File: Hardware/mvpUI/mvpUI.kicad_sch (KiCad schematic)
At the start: 0 parts

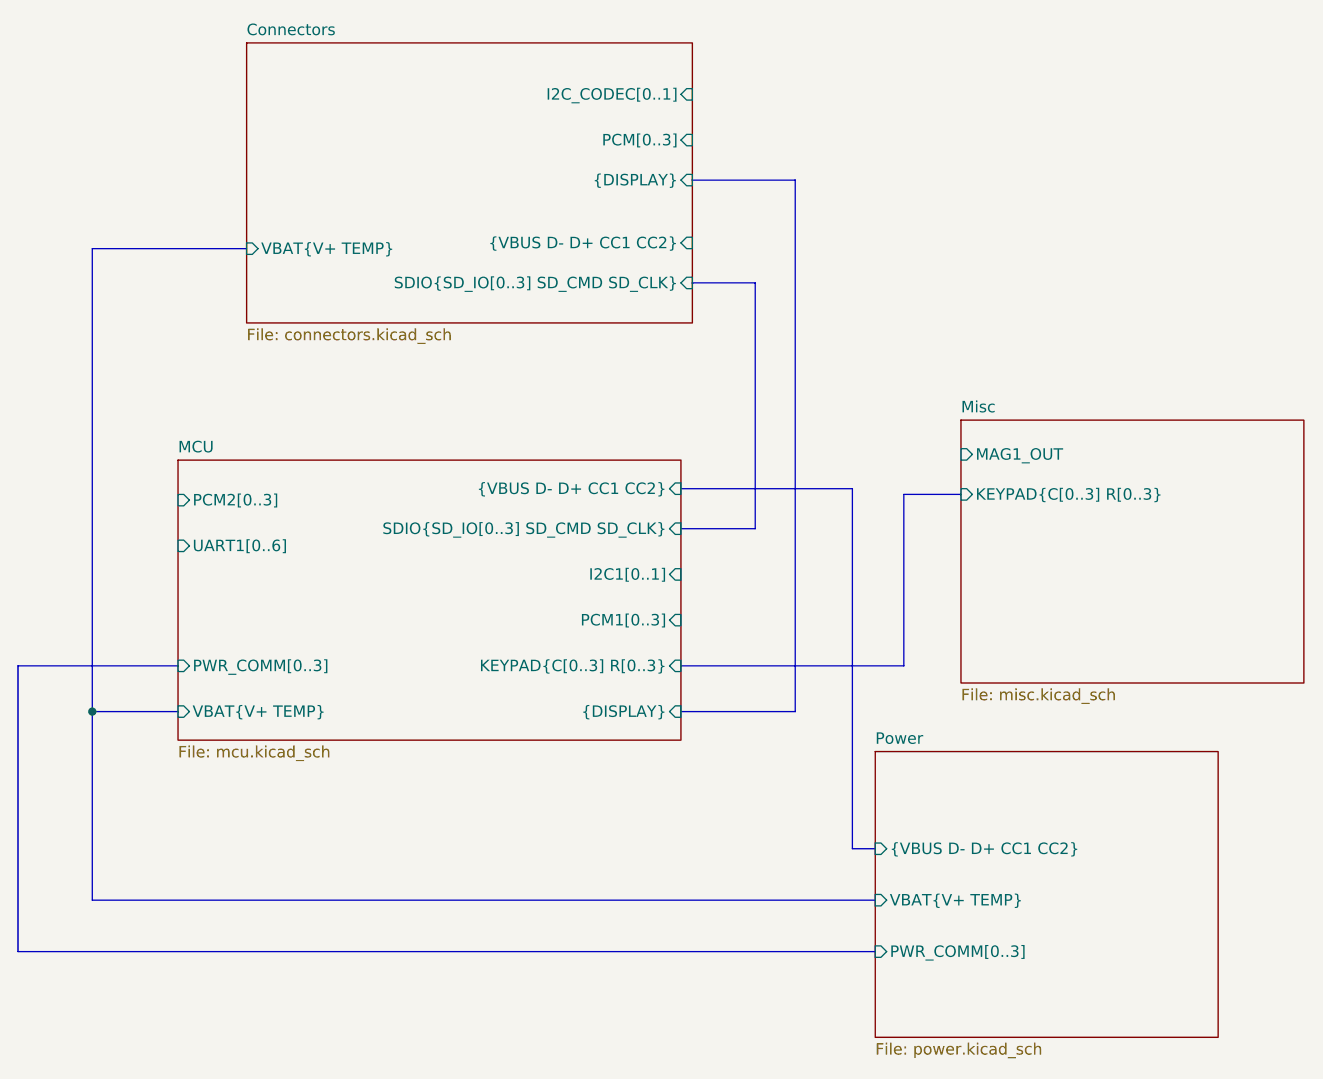
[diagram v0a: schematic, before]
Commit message: Getting there...
Just need logic and power planes for the most part (and verify everything once more)
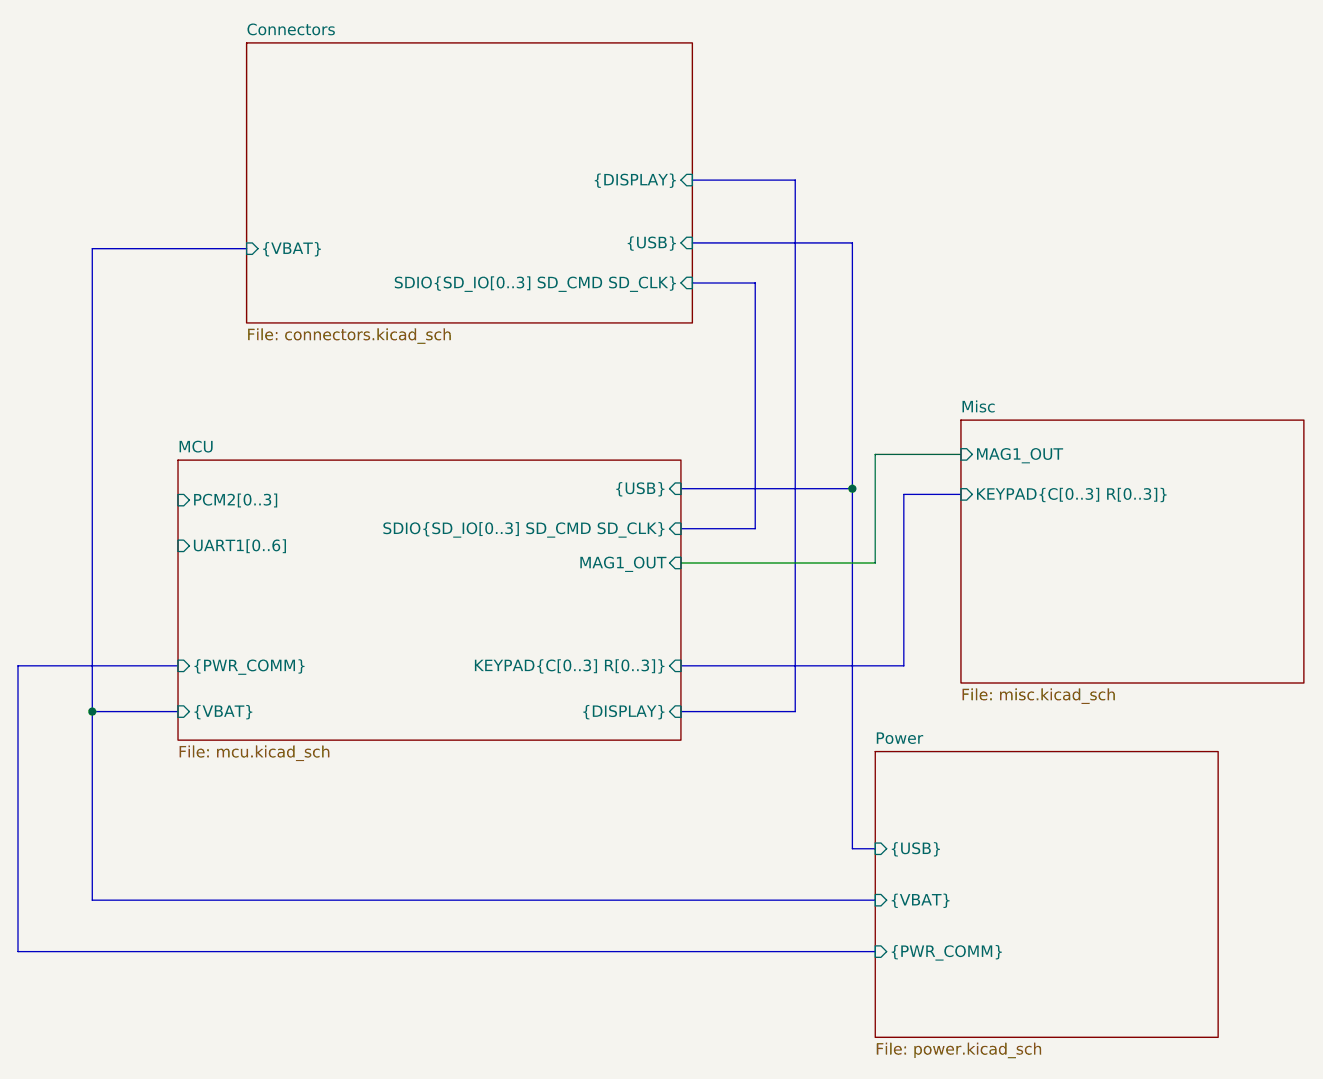
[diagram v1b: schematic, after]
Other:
- sheet Connectors ports: added {USB}, {VBAT}; removed I2C_CODEC[0..1], PCM[0..3], VBAT{V+ TEMP}, {VBUS D- D+ CC1 CC2}
- sheet MCU ports: added KEYPAD{C[0..3] R[0..3]}, MAG1_OUT, {PWR_COMM}, {USB}, {VBAT}; removed I2C1[0..1], KEYPAD{C[0..3] R[0..3}, PCM1[0..3], PWR_COMM[0..3], VBAT{V+ TEMP}, {VBUS D- D+ CC1 CC2}
- sheet Misc ports: added KEYPAD{C[0..3] R[0..3]}; removed KEYPAD{C[0..3] R[0..3}
- sheet Power ports: added {PWR_COMM}, {USB}, {VBAT}; removed PWR_COMM[0..3], VBAT{V+ TEMP}, {VBUS D- D+ CC1 CC2}
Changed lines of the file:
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@@
 (kicad_sch (version 20230121) (generator eeschema)
   (paper "A4")
+  (bus_alias "USB" (members "VBUS" "D+" "D-" "CC1" "CC2"))
+  (bus_alias "VBAT" (members "V+" "TEMP"))
+  (junction (at 132.715 95.25) (diameter 0) (color 0 0 0 0)
+  )
   (junction (at 48.26 120.015) (diameter 0) (color 0 0 0 0)
   )
@@
   )
   (bus (pts (xy 48.26 140.97) (xy 135.255 140.97))
+    (stroke (width 0) (type default))
+  )
+  (bus (pts (xy 132.715 95.25) (xy 132.715 67.945))
     (stroke (width 0) (type default))
   )
@@
     (stroke (width 0) (type default))
   )
+  (wire (pts (xy 135.255 103.505) (xy 135.255 91.44))
+    (stroke (width 0) (type default))
+  )
   (bus (pts (xy 48.26 68.58) (xy 48.26 120.015))
     (stroke (width 0) (type default))
@@
     (stroke (width 0) (type default))
   )
+  (bus (pts (xy 132.715 67.945) (xy 114.935 67.945))
+    (stroke (width 0) (type default))
+  )
+  (wire (pts (xy 135.255 91.44) (xy 144.78 91.44))
+    (stroke (width 0) (type default))
+  )
   (bus (pts (xy 138.43 95.885) (xy 138.43 114.935))
+    (stroke (width 0) (type default))
+  )
+  (wire (pts (xy 113.665 103.505) (xy 135.255 103.505))
     (stroke (width 0) (type default))
   )
@@
       (effects (font (size 1.27 1.27)) (justify left top))
     )
-    (pin "I2C1[0..1]" input (at 113.665 104.775 0)
-      (effects (font (size 1.27 1.27)) (justify right))
-    )
     (pin "UART1[0..6]" input (at 57.785 101.6 180)
       (effects (font (size 1.27 1.27)) (justify left))
     )
-    (pin "{VBUS D- D+ CC1 CC2}" input (at 113.665 95.25 0)
-      (effects (font (size 1.27 1.27)) (justify right))
-    )
-    (pin "PCM1[0..3]" input (at 113.665 109.855 0)
+    (pin "{USB}" input (at 113.665 95.25 0)
       (effects (font (size 1.27 1.27)) (justify right))
     )
@@
       (effects (font (size 1.27 1.27)) (justify left))
     )
-    (pin "KEYPAD{C[0..3] R[0..3}" input (at 113.665 114.935 0)
+    (pin "KEYPAD{C[0..3] R[0..3]}" input (at 113.665 114.935 0)
       (effects (font (size 1.27 1.27)) (justify right))
     )
@@
       (effects (font (size 1.27 1.27)) (justify right))
     )
-    (pin "VBAT{V+ TEMP}" input (at 57.785 120.015 180)
+    (pin "{VBAT}" input (at 57.785 120.015 180)
       (effects (font (size 1.27 1.27)) (justify left))
     )
-    (pin "PWR_COMM[0..3]" input (at 57.785 114.935 180)
+    (pin "{PWR_COMM}" input (at 57.785 114.935 180)
       (effects (font (size 1.27 1.27)) (justify left))
     )
+    (pin "MAG1_OUT" input (at 113.665 103.505 0)
+      (effects (font (size 1.27 1.27)) (justify right))
+    )
     (instances
-      (project "layout"
+      (project "mvpUI"
         (path "/194f3002-cdfe-4c02-828d-0f9a04309e79" (page "5"))
       )
@@
       (effects (font (size 1.27 1.27)) (justify left top))
     )
-    (pin "{VBUS D- D+ CC1 CC2}" input (at 114.935 67.945 0)
+    (pin "{USB}" input (at 114.935 67.945 0)
       (effects (font (size 1.27 1.27)) (justify right))
     )
@@
       (effects (font (size 1.27 1.27)) (justify right))
     )
-    (pin "VBAT{V+ TEMP}" input (at 65.405 68.58 180)
+    (pin "{VBAT}" input (at 65.405 68.58 180)
       (effects (font (size 1.27 1.27)) (justify left))
-    )
-    (pin "I2C_CODEC[0..1]" input (at 114.935 51.435 0)
-      (effects (font (size 1.27 1.27)) (justify right))
-    )
-    (pin "PCM[0..3]" input (at 114.935 56.515 0)
-      (effects (font (size 1.27 1.27)) (justify right))
     )
     (pin "{DISPLAY}" input (at 114.935 60.96 0)
@@
     )
     (instances
-      (project "layout"
+      (project "mvpUI"
         (path "/194f3002-cdfe-4c02-828d-0f9a04309e79" (page "3"))
       )
@@
       (effects (font (size 1.27 1.27)) (justify left top))
     )
-    (pin "VBAT{V+ TEMP}" input (at 135.255 140.97 180)
+    (pin "{VBAT}" input (at 135.255 140.97 180)
       (effects (font (size 1.27 1.27)) (justify left))
     )
-    (pin "{VBUS D- D+ CC1 CC2}" input (at 135.255 135.255 180)
+    (pin "{USB}" input (at 135.255 135.255 180)
       (effects (font (size 1.27 1.27)) (justify left))
     )
-    (pin "PWR_COMM[0..3]" input (at 135.255 146.685 180)
+    (pin "{PWR_COMM}" input (at 135.255 146.685 180)
       (effects (font (size 1.27 1.27)) (justify left))
     )
     (instances
-      (project "layout"
+      (project "mvpUI"
         (path "/194f3002-cdfe-4c02-828d-0f9a04309e79" (page "6"))
       )
@@
       (effects (font (size 1.27 1.27)) (justify left))
     )
-    (pin "KEYPAD{C[0..3] R[0..3}" input (at 144.78 95.885 180)
+    (pin "KEYPAD{C[0..3] R[0..3]}" input (at 144.78 95.885 180)
       (effects (font (size 1.27 1.27)) (justify left))
     )
     (instances
-      (project "layout"
+      (project "mvpUI"
         (path "/194f3002-cdfe-4c02-828d-0f9a04309e79" (page "6"))
       )
